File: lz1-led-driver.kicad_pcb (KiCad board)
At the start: 2 copper layers, 80 x 20.5 mm, 41 parts, among them J1 BarrelJack_3167288, J2 USB4105-GF-A, U1 MP2483DQ-LF-P, U2 AP62301Z6-7, U3 SM02B-SRSS-TB-LF-SN, U4 SM02B-SRSS-TB-LF-SN

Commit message: Bump revision to 1.1. Update the PCB signage
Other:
- board text added: "EZ1 LED Driver rev.1.1.0 05/2023"
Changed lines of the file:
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@@
     (effects (font (size 0.7 0.7) (thickness 0.15)))
   )
-  (gr_text "1050nm IR LED Driver \nrev.1.0.0 04/2023" (at 129.506392 46.504296) (layer "B.Mask")
+  (gr_text "EZ1 LED Driver \nrev.1.1.0 05/2023" (at 129.506392 46.504296) (layer "B.Mask")
     (effects (font (size 0.5 0.5) (thickness 0.125)) (justify left mirror))
   )

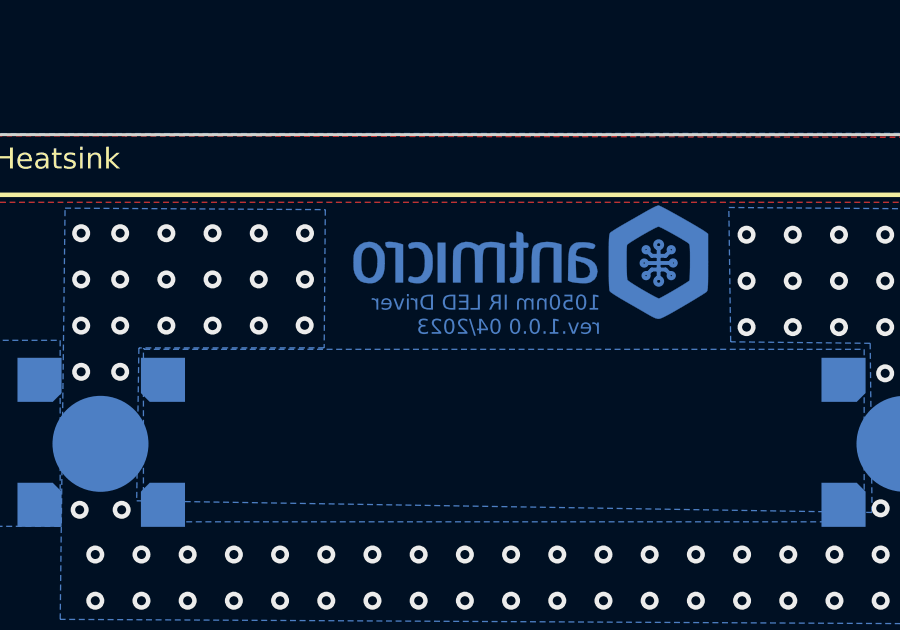
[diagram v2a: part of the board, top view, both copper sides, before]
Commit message: README updates, board naming unification
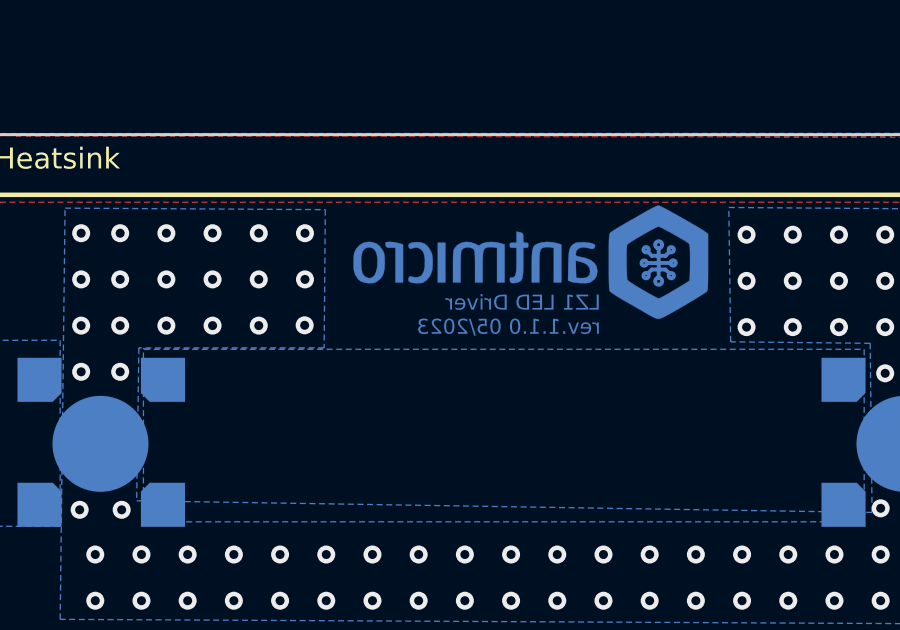
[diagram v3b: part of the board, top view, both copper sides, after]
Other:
- board text added: "LZ1 LED Driver rev.1.1.0 05/2023"
- board text removed: "1050nm IR LED Driver rev.1.0.0 04/2023"
- board text removed: "EZ1 LED Driver rev.1.1.0 05/2023"
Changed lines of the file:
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@@
   (gr_rect (start 109.075 43.025) (end 143.525 58.775) (layer "F.Mask") (width 0.15) (fill solid))
   (gr_rect (start 85 40.5) (end 165 61) (layer "Edge.Cuts") (width 0.1) (fill none))
-  (gr_text "1050nm IR LED Driver \nrev.1.0.0 04/2023" (at 129.506392 46.504296) (layer "B.Cu")
+  (gr_text "LZ1 LED Driver \nrev.1.1.0 05/2023" (at 129.506392 46.504296) (layer "B.Cu")
     (effects (font (size 0.5 0.5) (thickness 0.125)) (justify left mirror))
   )
@@
     (effects (font (size 0.7 0.7) (thickness 0.15)))
   )
-  (gr_text "EZ1 LED Driver \nrev.1.1.0 05/2023" (at 129.506392 46.504296) (layer "B.Mask")
+  (gr_text "LZ1 LED Driver \nrev.1.1.0 05/2023" (at 129.506392 46.504296) (layer "B.Mask")
     (effects (font (size 0.5 0.5) (thickness 0.125)) (justify left mirror))
   )
